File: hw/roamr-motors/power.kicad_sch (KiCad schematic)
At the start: 25 parts, among them U5 SGM2212-3.3XKC3G_TR

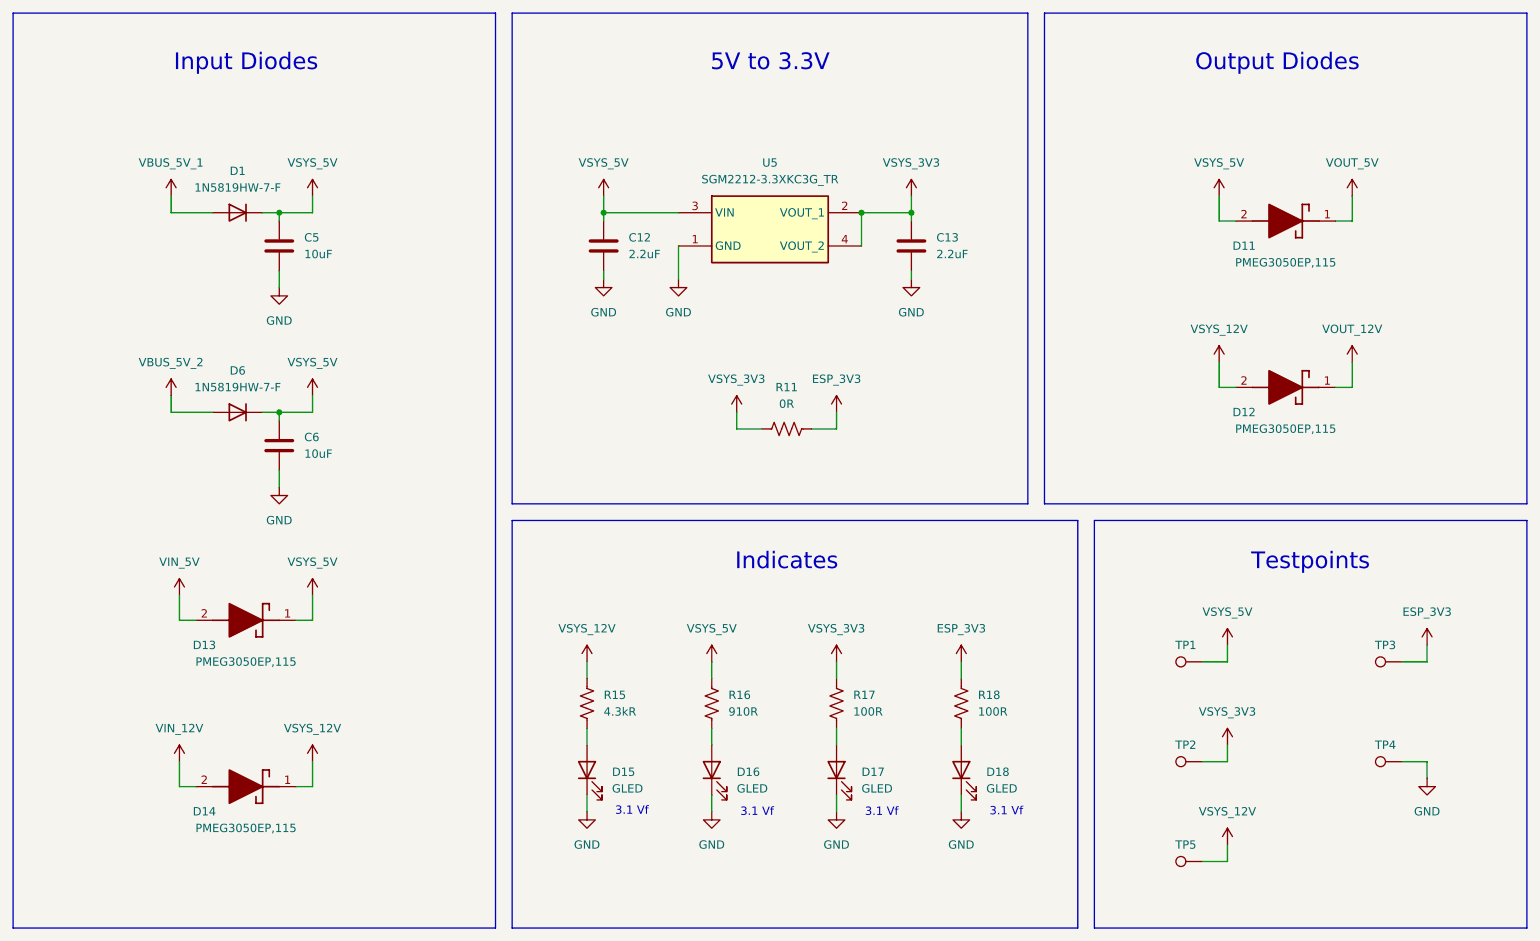
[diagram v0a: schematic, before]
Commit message: added all footprints, starting layout properly
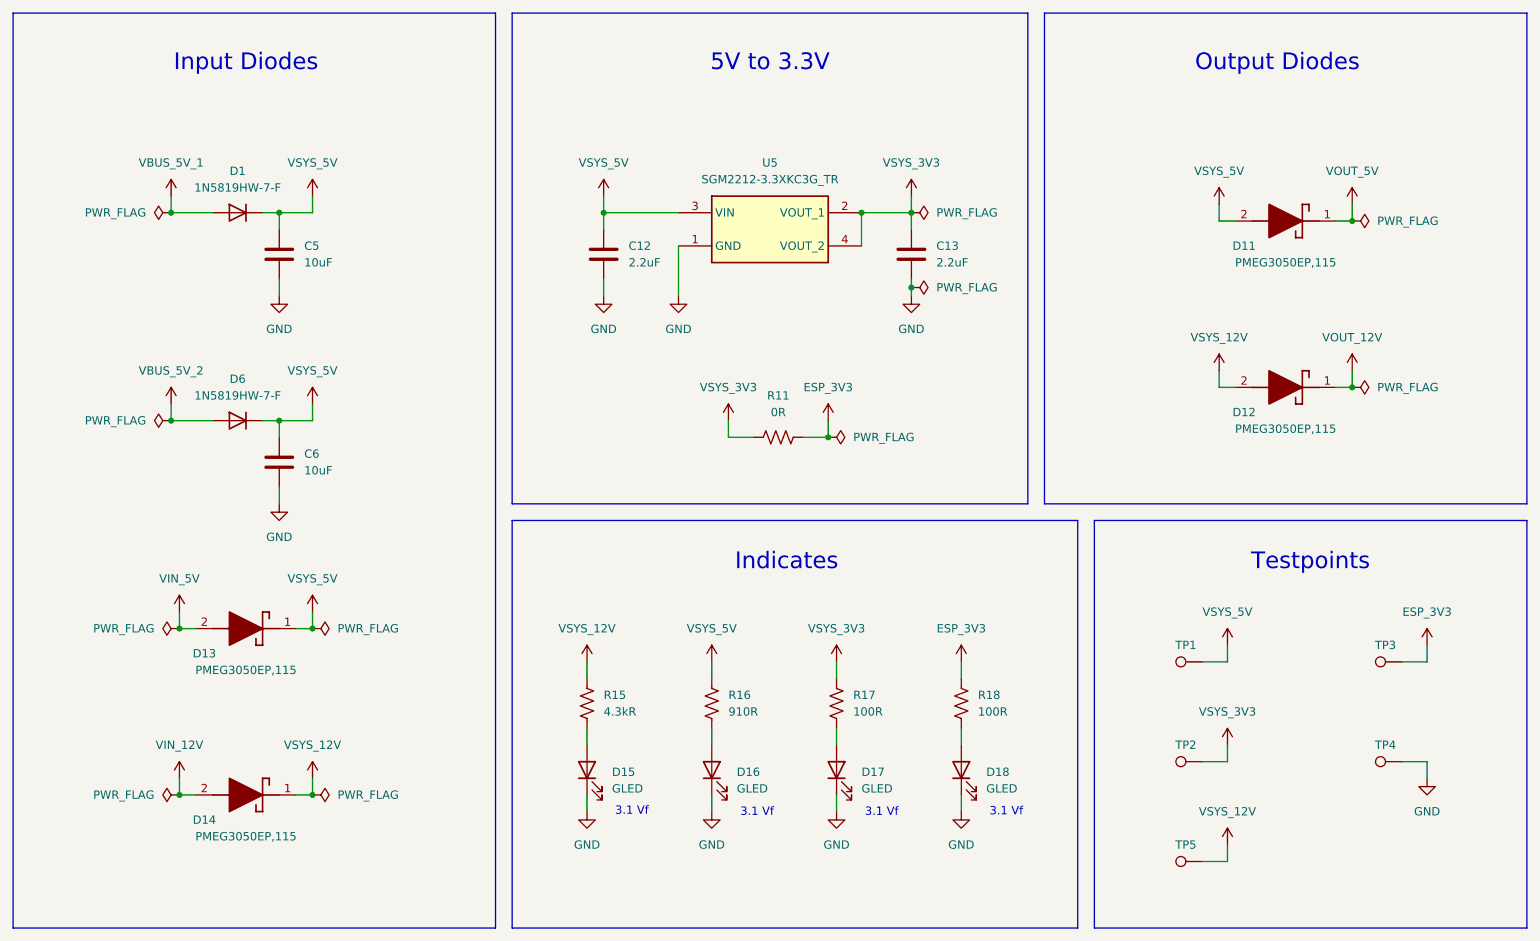
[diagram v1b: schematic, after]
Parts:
- D1, D6: footprint (none) -> 1N5819HW_7_F:SOD3715X145N
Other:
- moved on the sheet: C12, C13, C5, C6, D13, D14, D6, R11

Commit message: some more layout
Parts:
- removed D1, D6: 1N5819HW-7-F, 1N5819HW_7_F:SOD3715X145N, symbol Device:D
- added D1, D6: 1N5819HW-7-F, 1N5819HW_7_F:SOD3715X145N, symbol 1N5819HW-7-F:1N5819HW-7-F
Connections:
- net VBUS_5V_1: now also D1.A
- net VBUS_5V_2: now also D6.A
- net VSYS_5V: now also D1.C, D6.C
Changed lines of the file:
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@@
 	(wire
 		(pts
-			(xy 48.26 55.88) (xy 54.61 55.88)
+			(xy 48.26 55.88) (xy 52.07 55.88)
 		)
 		(stroke
@@
 	(wire
 		(pts
-			(xy 48.26 87.63) (xy 54.61 87.63)
+			(xy 48.26 87.63) (xy 52.07 87.63)
 		)
 		(stroke
@@
 	)
 	(symbol
-		(lib_id "Device:D")
-		(at 58.42 55.88 0)
-		(mirror y)
-		(unit 1)
-		(exclude_from_sim no)
-		(in_bom yes)
-		(on_board yes)
-		(dnp no)
-		(fields_autoplaced yes)
-		(property "Reference" "D1"
-			(at 58.42 49.53 0)
-			(effects
-				(font
-					(size 1.27 1.27)
-				)
-			)
-		)
-		(property "Value" "1N5819HW-7-F"
-			(at 58.42 52.07 0)
-			(effects
-				(font
-					(size 1.27 1.27)
-				)
-			)
-		)
-		(property "Footprint" "1N5819HW_7_F:SOD3715X145N"
-			(at 58.42 55.88 0)
-			(effects
-				(font
-					(size 1.27 1.27)
-				)
-				(hide yes)
-			)
-		)
-		(property "Datasheet" "~"
-			(at 58.42 55.88 0)
-			(effects
-				(font
-					(size 1.27 1.27)
-				)
-				(hide yes)
-			)
-		)
-		(property "Description" "Diode"
-			(at 58.42 55.88 0)
-			(effects
-				(font
-					(size 1.27 1.27)
-				)
-				(hide yes)
-			)
-		)
-		(property "Sim.Device" "D"
-			(at 58.42 55.88 0)
-			(effects
-				(font
-					(size 1.27 1.27)
-				)
-				(hide yes)
-			)
-		)
-		(property "Sim.Pins" "1=K 2=A"
-			(at 58.42 55.88 0)
-			(effects
-				(font
-					(size 1.27 1.27)
-				)
-				(hide yes)
-			)
-		)
-		(pin "1"
-		)
-		(pin "2"
-		)
-		(instances
-			(project "roamr-motors"
-				(path "/db664d1d-d972-4e66-af85-94b6971e1c6e/cd542ca1-7cb6-4383-96e9-21f6e9c0c0a4"
-					(reference "D1")
-					(unit 1)
-				)
-			)
-		)
-	)
-	(symbol
 		(lib_id "Device:C")
 		(at 64.77 93.98 0)
@@
 	)
 	(symbol
-		(lib_id "Device:D")
-		(at 58.42 87.63 0)
-		(mirror y)
-		(unit 1)
-		(exclude_from_sim no)
-		(in_bom yes)
-		(on_board yes)
-		(dnp no)
-		(fields_autoplaced yes)
-		(property "Reference" "D6"
-			(at 58.42 81.28 0)
-			(effects
-				(font
-					(size 1.27 1.27)
-				)
-			)
-		)
-		(property "Value" "1N5819HW-7-F"
-			(at 58.42 83.82 0)
-			(effects
-				(font
-					(size 1.27 1.27)
-				)
-			)
-		)
-		(property "Footprint" "1N5819HW_7_F:SOD3715X145N"
-			(at 58.42 87.63 0)
-			(effects
-				(font
-					(size 1.27 1.27)
-				)
-				(hide yes)
-			)
-		)
-		(property "Datasheet" "~"
-			(at 58.42 87.63 0)
-			(effects
-				(font
-					(size 1.27 1.27)
-				)
-				(hide yes)
-			)
-		)
-		(property "Description" "Diode"
-			(at 58.42 87.63 0)
-			(effects
-				(font
-					(size 1.27 1.27)
-				)
-				(hide yes)
-			)
-		)
-		(property "Sim.Device" "D"
-			(at 58.42 87.63 0)
-			(effects
-				(font
-					(size 1.27 1.27)
-				)
-				(hide yes)
-			)
-		)
-		(property "Sim.Pins" "1=K 2=A"
-			(at 58.42 87.63 0)
-			(effects
-				(font
-					(size 1.27 1.27)
-				)
-				(hide yes)
-			)
-		)
-		(pin "1"
-		)
-		(pin "2"
-		)
-		(instances
-			(project "roamr-motors"
-				(path "/db664d1d-d972-4e66-af85-94b6971e1c6e/cd542ca1-7cb6-4383-96e9-21f6e9c0c0a4"
-					(reference "D6")
-					(unit 1)
-				)
-			)
-		)
-	)
-	(symbol
 		(lib_id "PMEG3050EP_115:PMEG3050EP,115")
 		(at 228.6 57.15 180)
@@
 	)
 	(symbol
+		(lib_id "1N5819HW-7-F:1N5819HW-7-F")
+		(at 57.15 55.88 0)
+		(unit 1)
+		(exclude_from_sim no)
+		(in_bom yes)
+		(on_board yes)
+		(dnp no)
+		(property "Reference" "D1"
+			(at 57.15 49.53 0)
+			(effects
+				(font
+					(size 1.27 1.27)
+				)
+			)
+		)
+		(property "Value" "1N5819HW-7-F"
+			(at 59.69 52.07 0)
+			(effects
+				(font
+					(size 1.27 1.27)
+				)
+			)
+		)
+		(property "Footprint" "1N5819HW_7_F:SOD3715X145N"
+			(at 57.15 55.88 0)
+			(effects
+				(font
+					(size 1.27 1.27)
+				)
+				(justify bottom)
+				(hide yes)
+			)
+		)
+		(property "Datasheet" ""
+			(at 57.15 55.88 0)
+			(effects
+				(font
+					(size 1.27 1.27)
+				)
+				(hide yes)
+			)
+		)
+		(property "Description" ""
+			(at 57.15 55.88 0)
+			(effects
+				(font
+					(size 1.27 1.27)
+				)
+				(hide yes)
+			)
+		)
+		(property "PARTREV" "18-2"
+			(at 57.15 55.88 0)
+			(effects
+				(font
+					(size 1.27 1.27)
+				)
+				(justify bottom)
+				(hide yes)
+			)
+		)
+		(property "STANDARD" "IPC-7351B"
+			(at 57.15 55.88 0)
+			(effects
+				(font
+					(size 1.27 1.27)
+				)
+				(justify bottom)
+				(hide yes)
+			)
+		)
+		(property "MANUFACTURER" "Diodes Inc."
+			(at 57.15 55.88 0)
+			(effects
+				(font
+					(size 1.27 1.27)
+				)
+				(justify bottom)
+				(hide yes)
+			)
+		)
+		(pin "A"
+		)
+		(pin "C"
+		)
+		(instances
+			(project "roamr-motors"
+				(path "/db664d1d-d972-4e66-af85-94b6971e1c6e/cd542ca1-7cb6-4383-96e9-21f6e9c0c0a4"
+					(reference "D1")
+					(unit 1)
+				)
+			)
+		)
+	)
+	(symbol
 		(lib_id "power:VBUS")
 		(at 111.76 124.46 0)
@@
 					(unit 1)
 				)
+			)
+		)
+	)
+	(symbol
+		(lib_id "1N5819HW-7-F:1N5819HW-7-F")
+		(at 57.15 87.63 0)
+		(unit 1)
+		(exclude_from_sim no)
+		(in_bom yes)
+		(on_board yes)
+		(dnp no)
+		(property "Reference" "D6"
+			(at 57.15 81.28 0)
+			(effects
+				(font
+					(size 1.27 1.27)
+				)
+			)
+		)
+		(property "Value" "1N5819HW-7-F"
+			(at 58.42 83.82 0)
+			(effects
+				(font
+					(size 1.27 1.27)
+				)
+			)
+		)
+		(property "Footprint" "1N5819HW_7_F:SOD3715X145N"
+			(at 57.15 87.63 0)
+			(effects
+				(font
+					(size 1.27 1.27)
+				)
+				(justify bottom)
+				(hide yes)
+			)
+		)
+		(property "Datasheet" ""
+			(at 57.15 87.63 0)
+			(effects
+				(font
+					(size 1.27 1.27)
+				)
+				(hide yes)
+			)
+		)
+		(property "Description" ""
+			(at 57.15 87.63 0)
+			(effects
+				(font
+					(size 1.27 1.27)
+				)
+				(hide yes)
+			)
+		)
+		(property "PARTREV" "18-2"
+			(at 57.15 87.63 0)
+			(effects
+				(font
+					(size 1.27 1.27)
+				)
+				(justify bottom)
+				(hide yes)
+			)
+		)
+		(property "STANDARD" "IPC-7351B"
+			(at 57.15 87.63 0)
+			(effects
+				(font
+					(size 1.27 1.27)
+				)
+				(justify bottom)
+				(hide yes)
+			)
+		)
+		(property "MANUFACTURER" "Diodes Inc."
+			(at 57.15 87.63 0)
+			(effects
+				(font
+					(size 1.27 1.27)
+				)
+				(justify bottom)
+				(hide yes)
+			)
+		)
+		(pin "A"
+		)
+		(pin "C"
+		)
+		(instances
+			(project ""
+				(path "/db664d1d-d972-4e66-af85-94b6971e1c6e/cd542ca1-7cb6-4383-96e9-21f6e9c0c0a4"
+					(reference "D6")
+					(unit 1)
+				)

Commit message: more layout, i think i get do it on one side
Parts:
- renumbered C5 to C1, C6 to C2, C12 to C3, C13 to C4, D6 to D10, D13 to D11, D14 to D12, D15 to D13, D16 to D14, D17 to D15, D18 to D16, D11 to D17, D12 to D18, D1 to D9, R15 to R5, R16 to R6, R11 to R7, R17 to R8, R18 to R9, TP5 to TP3, TP3 to TP4, TP4 to TP5, U5 to U1

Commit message: outputs and last minute updates
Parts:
- D10, D9: Manufacturer_Part_Number (none) -> 1N5819HW-7-F
- D13, D14, D15, D16: Manufacturer_Part_Number (none) -> KT-0603G
- TP5: Manufacturer_Part_Number (none) -> 5005-5009
